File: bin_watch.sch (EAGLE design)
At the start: 90 parts, among them IC1 MEGA48/88/168-AU, J1 USB3100-XX-X_REVB, Q1 32.768kHz, T1 2N7002BKV, T2 2N7002BKV, T3 2N7002BKV, T4 2N7002BKV, T5 PMDT670UPE, T6 PMDT670UPE, T7 PMDT670UPE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

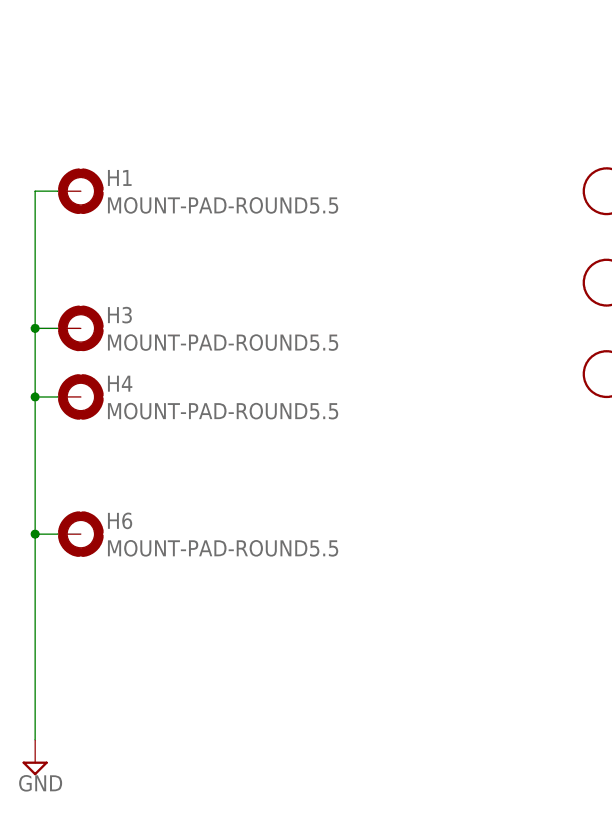
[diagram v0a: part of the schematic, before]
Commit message: Removed mounting holes
Saved a lot more space
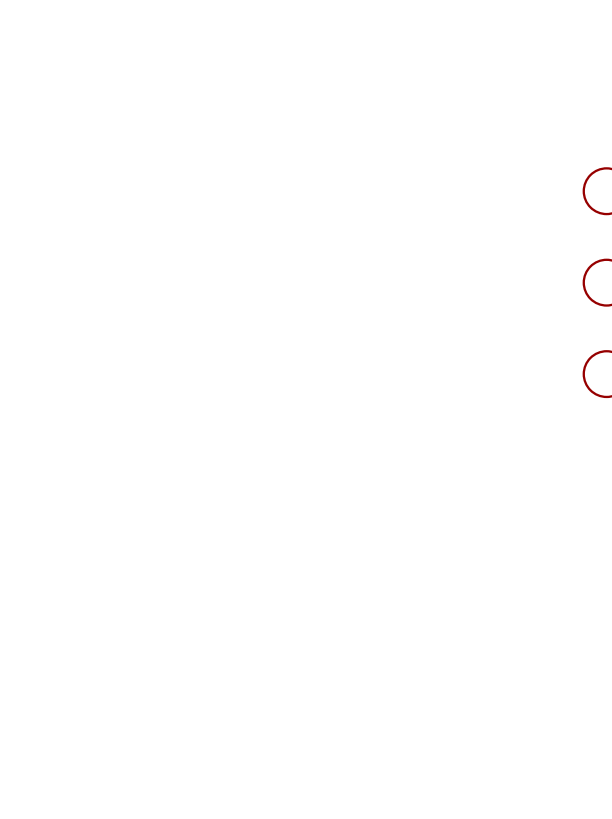
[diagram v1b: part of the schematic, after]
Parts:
- removed H1, H3, H4, H6: MOUNT-PAD-ROUND5.5, holes:MOUNT-PAD-ROUND5.5
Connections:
- net GND: no longer H1.MOUNT, H3.MOUNT, H4.MOUNT, H6.MOUNT
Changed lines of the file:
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@@
 <part name="SUPPLY14" library="supply2" library_urn="urn:adsk.eagle:library:372" deviceset="GND" device=""/>
 <part name="SUPPLY15" library="supply2" library_urn="urn:adsk.eagle:library:372" deviceset="GND" device=""/>
-<part name="H1" library="holes" library_urn="urn:adsk.eagle:library:237" deviceset="MOUNT-PAD-ROUND" device="5.5" value="MOUNT-PAD-ROUND5.5"/>
-<part name="H3" library="holes" library_urn="urn:adsk.eagle:library:237" deviceset="MOUNT-PAD-ROUND" device="5.5" value="MOUNT-PAD-ROUND5.5"/>
-<part name="H4" library="holes" library_urn="urn:adsk.eagle:library:237" deviceset="MOUNT-PAD-ROUND" device="5.5" value="MOUNT-PAD-ROUND5.5"/>
-<part name="H6" library="holes" library_urn="urn:adsk.eagle:library:237" deviceset="MOUNT-PAD-ROUND" device="5.5" value="MOUNT-PAD-ROUND5.5"/>
-<part name="SUPPLY16" library="supply2" library_urn="urn:adsk.eagle:library:372" deviceset="GND" device=""/>
 <part name="T1" library="nxp_60" deviceset="2N7002BK" device="V"/>
 <part name="T2" library="nxp_60" deviceset="2N7002BK" device="V"/>
@@
 <instance part="SUPPLY14" gate="GND" x="254" y="20.32"/>
 <instance part="SUPPLY15" gate="GND" x="299.72" y="223.52"/>
-<instance part="H1" gate="G$1" x="30.48" y="-53.34"/>
-<instance part="H3" gate="G$1" x="30.48" y="-68.58"/>
-<instance part="H4" gate="G$1" x="30.48" y="-76.2"/>
-<instance part="H6" gate="G$1" x="30.48" y="-91.44"/>
-<instance part="SUPPLY16" gate="GND" x="25.4" y="-116.84"/>
 <instance part="T1" gate="-1" x="180.34" y="45.72"/>
 <instance part="T1" gate="-2" x="190.5" y="27.94"/>
@@
 </segment>
 <segment>
-<pinref part="H1" gate="G$1" pin="MOUNT"/>
-<wire x1="27.94" y1="-53.34" x2="25.4" y2="-53.34" width="0.1524" layer="91"/>
-<pinref part="SUPPLY16" gate="GND" pin="GND"/>
-<wire x1="25.4" y1="-53.34" x2="25.4" y2="-68.58" width="0.1524" layer="91"/>
-<wire x1="25.4" y1="-68.58" x2="25.4" y2="-76.2" width="0.1524" layer="91"/>
-<wire x1="25.4" y1="-76.2" x2="25.4" y2="-91.44" width="0.1524" layer="91"/>
-<wire x1="25.4" y1="-91.44" x2="25.4" y2="-114.3" width="0.1524" layer="91"/>
-<pinref part="H3" gate="G$1" pin="MOUNT"/>
-<wire x1="27.94" y1="-68.58" x2="25.4" y2="-68.58" width="0.1524" layer="91"/>
-<junction x="25.4" y="-68.58"/>
-<pinref part="H4" gate="G$1" pin="MOUNT"/>
-<wire x1="27.94" y1="-76.2" x2="25.4" y2="-76.2" width="0.1524" layer="91"/>
-<junction x="25.4" y="-76.2"/>
-<pinref part="H6" gate="G$1" pin="MOUNT"/>
-<wire x1="27.94" y1="-91.44" x2="25.4" y2="-91.44" width="0.1524" layer="91"/>
-<junction x="25.4" y="-91.44"/>
-</segment>
-<segment>

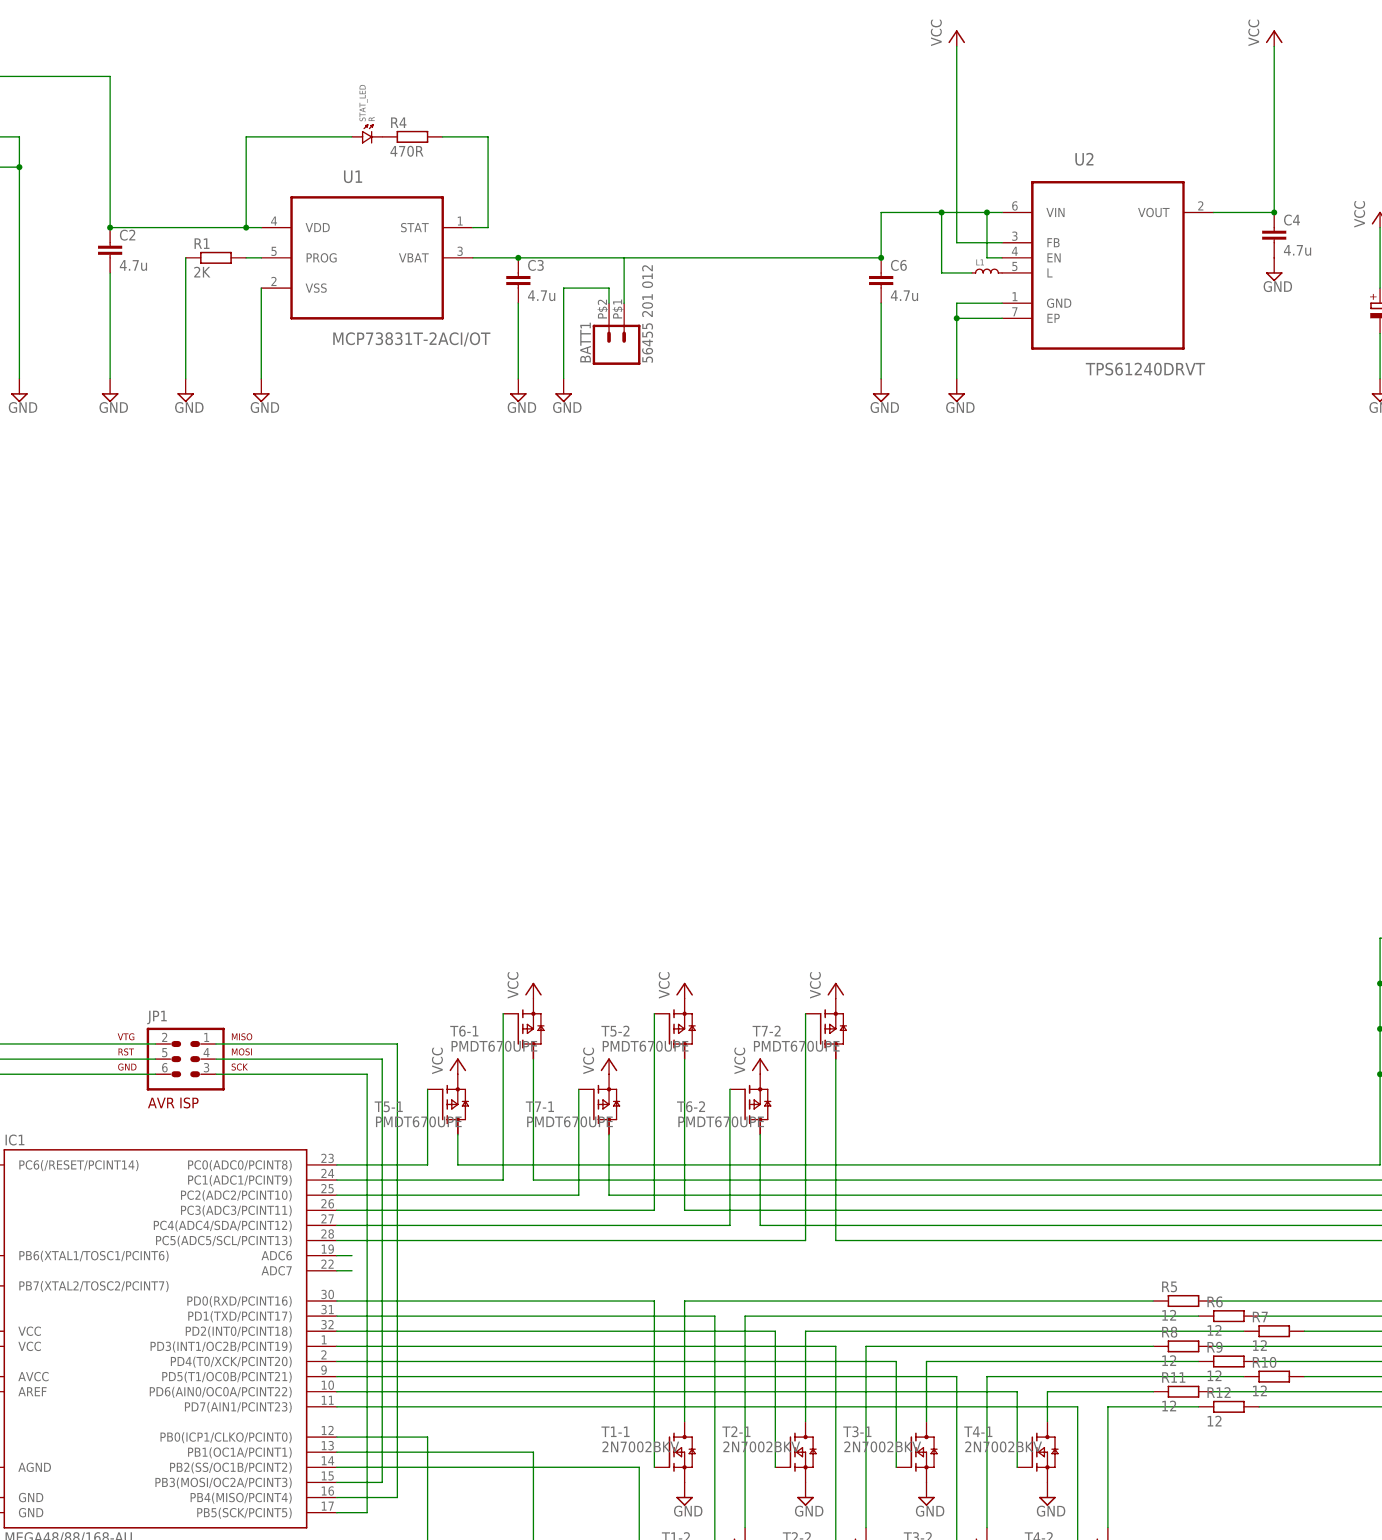
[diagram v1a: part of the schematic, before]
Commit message: Added charger isolation
When the battery is being charged, the Boost converter is powered directly from USB rather than through the charger.
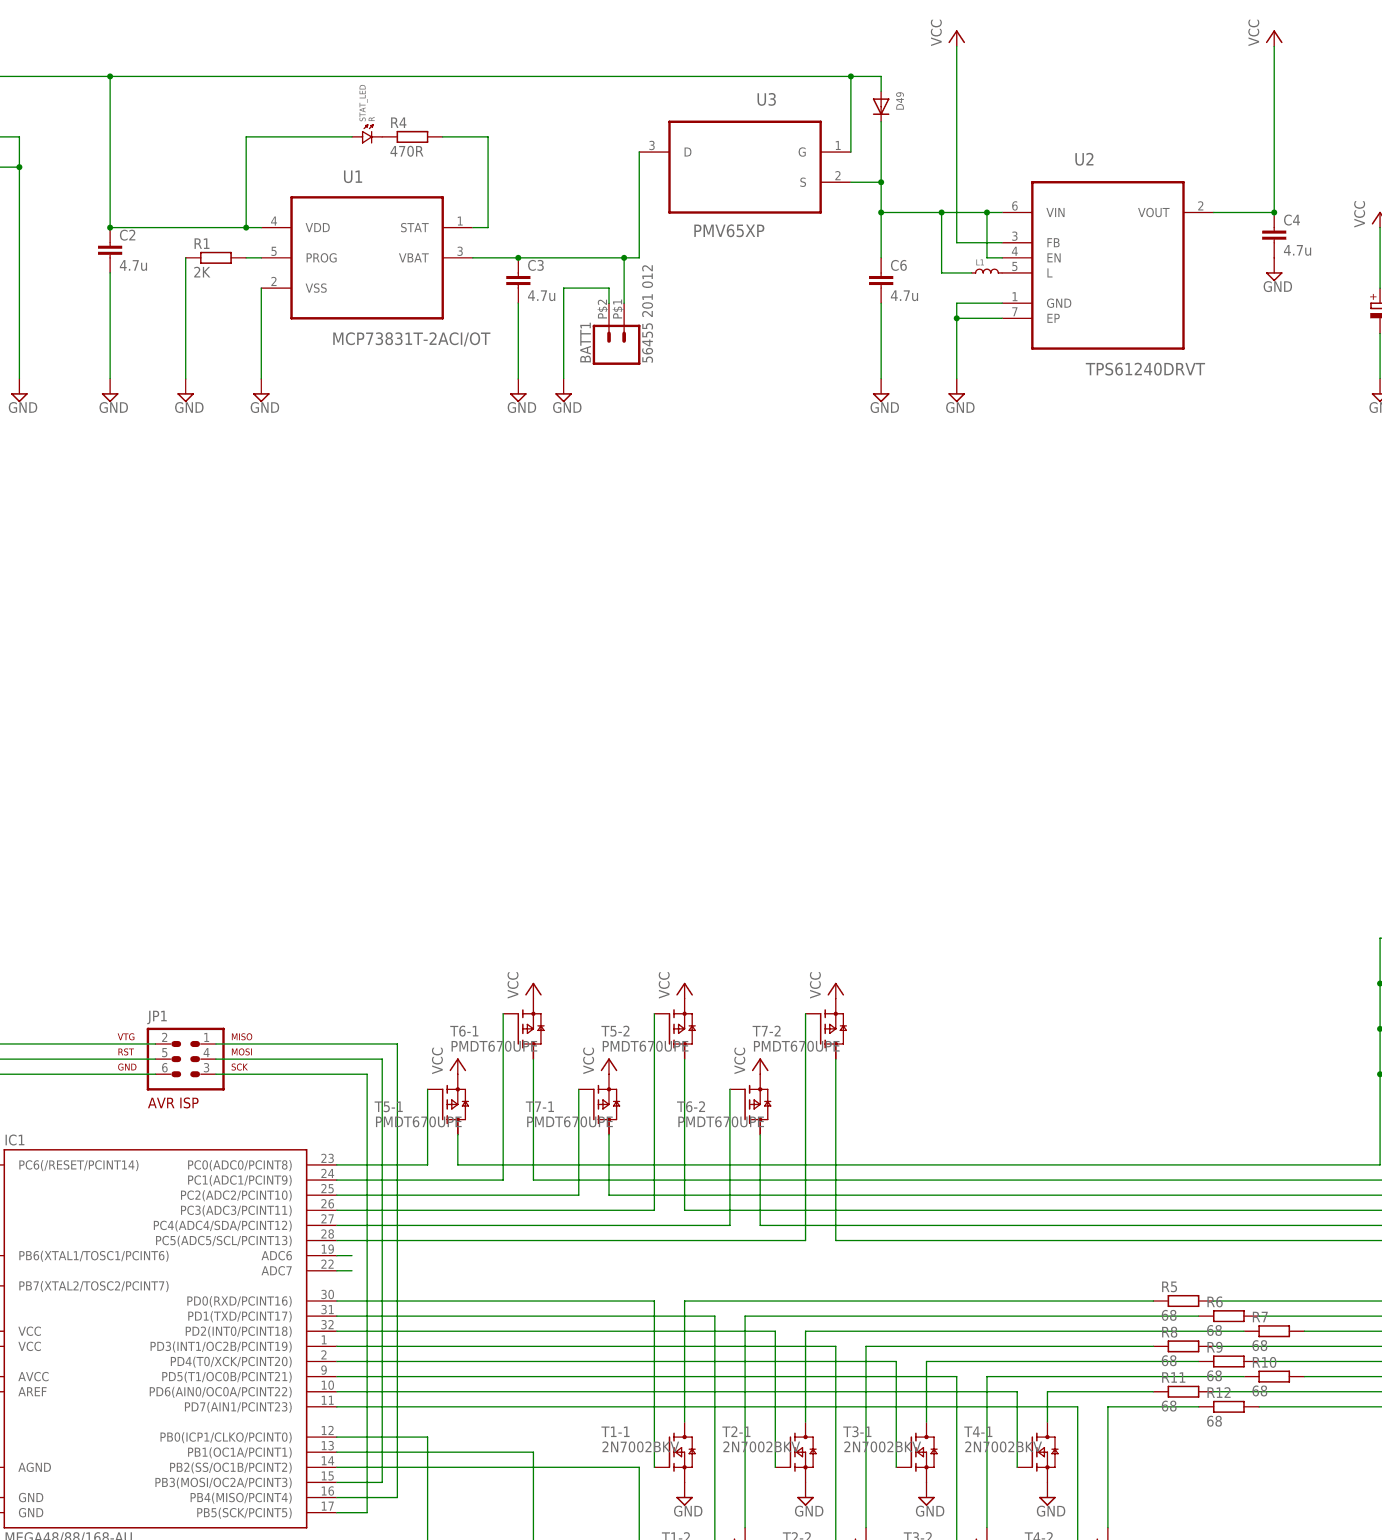
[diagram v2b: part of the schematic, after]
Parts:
- added D49: (no value), adafruit:DIODESOD-523
- added U3: PMV65XP, NXP_By_element14_Batch_1:PMV48XP
- R10, R11, R12, R5, R6, R7, R8, R9: value 12 -> 68
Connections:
- new net VIN: C6.1, D49.C, L1.1, U2.EN, U2.VIN, U3.S
- net VBATT: now also U3.D; no longer C6.1, L1.1, U2.EN, U2.VIN
- net VBUS: now also D49.A, U3.G
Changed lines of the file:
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@@
 <part name="P+9" library="supply1" library_urn="urn:adsk.eagle:library:371" deviceset="VCC" device=""/>
 <part name="C5" library="rcl" library_urn="urn:adsk.eagle:library:334" deviceset="CPOL-EU" device="B/3528-21R" package3d_urn="urn:adsk.eagle:package:23409/1" value="68u"/>
-<part name="R5" library="rcl" library_urn="urn:adsk.eagle:library:334" deviceset="R-EU_" device="R0603" package3d_urn="urn:adsk.eagle:package:23555/1" value="12"/>
-<part name="R6" library="rcl" library_urn="urn:adsk.eagle:library:334" deviceset="R-EU_" device="R0603" package3d_urn="urn:adsk.eagle:package:23555/1" value="12"/>
-<part name="R7" library="rcl" library_urn="urn:adsk.eagle:library:334" deviceset="R-EU_" device="R0603" package3d_urn="urn:adsk.eagle:package:23555/1" value="12"/>
-<part name="R8" library="rcl" library_urn="urn:adsk.eagle:library:334" deviceset="R-EU_" device="R0603" package3d_urn="urn:adsk.eagle:package:23555/1" value="12"/>
-<part name="R9" library="rcl" library_urn="urn:adsk.eagle:library:334" deviceset="R-EU_" device="R0603" package3d_urn="urn:adsk.eagle:package:23555/1" value="12"/>
-<part name="R10" library="rcl" library_urn="urn:adsk.eagle:library:334" deviceset="R-EU_" device="R0603" package3d_urn="urn:adsk.eagle:package:23555/1" value="12"/>
-<part name="R11" library="rcl" library_urn="urn:adsk.eagle:library:334" deviceset="R-EU_" device="R0603" package3d_urn="urn:adsk.eagle:package:23555/1" value="12"/>
-<part name="R12" library="rcl" library_urn="urn:adsk.eagle:library:334" deviceset="R-EU_" device="R0603" package3d_urn="urn:adsk.eagle:package:23555/1" value="12"/>
+<part name="R5" library="rcl" library_urn="urn:adsk.eagle:library:334" deviceset="R-EU_" device="R0603" package3d_urn="urn:adsk.eagle:package:23555/1" value="68"/>
+<part name="R6" library="rcl" library_urn="urn:adsk.eagle:library:334" deviceset="R-EU_" device="R0603" package3d_urn="urn:adsk.eagle:package:23555/1" value="68"/>
+<part name="R7" library="rcl" library_urn="urn:adsk.eagle:library:334" deviceset="R-EU_" device="R0603" package3d_urn="urn:adsk.eagle:package:23555/1" value="68"/>
+<part name="R8" library="rcl" library_urn="urn:adsk.eagle:library:334" deviceset="R-EU_" device="R0603" package3d_urn="urn:adsk.eagle:package:23555/1" value="68"/>
+<part name="R9" library="rcl" library_urn="urn:adsk.eagle:library:334" deviceset="R-EU_" device="R0603" package3d_urn="urn:adsk.eagle:package:23555/1" value="68"/>
+<part name="R10" library="rcl" library_urn="urn:adsk.eagle:library:334" deviceset="R-EU_" device="R0603" package3d_urn="urn:adsk.eagle:package:23555/1" value="68"/>
+<part name="R11" library="rcl" library_urn="urn:adsk.eagle:library:334" deviceset="R-EU_" device="R0603" package3d_urn="urn:adsk.eagle:package:23555/1" value="68"/>
+<part name="R12" library="rcl" library_urn="urn:adsk.eagle:library:334" deviceset="R-EU_" device="R0603" package3d_urn="urn:adsk.eagle:package:23555/1" value="68"/>
 <part name="U$1" library="adafruit" library_urn="urn:adsk.eagle:library:420" deviceset="FIDUCIAL" device=""/>
 <part name="U$2" library="adafruit" library_urn="urn:adsk.eagle:library:420" deviceset="FIDUCIAL" device=""/>
@@
 <part name="L1" library="standardparts" deviceset="RF-INDUCTOR" device=".0805"/>
 <part name="SUPPLY24" library="supply2" library_urn="urn:adsk.eagle:library:372" deviceset="GND" device=""/>
+<part name="U3" library="NXP_By_element14_Batch_1" deviceset="PMV48XP" device="" value="PMV65XP"/>
+<part name="D49" library="adafruit" library_urn="urn:adsk.eagle:library:420" deviceset="DIODE" device="SOD-523"/>
 </parts>
 <sheets>
@@
 <instance part="L1" gate="G$1" x="233.68" y="243.84"/>
 <instance part="SUPPLY24" gate="GND" x="215.9" y="223.52"/>
+<instance part="U3" gate="A" x="193.04" y="264.16" rot="MR0"/>
+<instance part="D49" gate="G$1" x="215.9" y="271.78" rot="R270"/>
 </instances>
 <busses>
@@
 <junction x="86.36" y="251.46"/>
 <pinref part="J1" gate="G$1" pin="VBUS"/>
-</segment>
-</net>
-<net name="VBATT" class="1">
-<segment>
-<pinref part="U1" gate="A" pin="VBAT"/>
-<pinref part="BATT1" gate="G$1" pin="1"/>
-<wire x1="147.32" y1="246.38" x2="154.94" y2="246.38" width="0.1524" layer="91"/>
-<wire x1="154.94" y1="246.38" x2="172.72" y2="246.38" width="0.1524" layer="91"/>
-<wire x1="172.72" y1="246.38" x2="172.72" y2="238.76" width="0.1524" layer="91"/>
-<pinref part="C3" gate="G$1" pin="1"/>
-<junction x="154.94" y="246.38"/>
+<pinref part="U3" gate="A" pin="G"/>
+<wire x1="86.36" y1="276.86" x2="210.82" y2="276.86" width="0.1524" layer="91"/>
+<wire x1="210.82" y1="276.86" x2="210.82" y2="264.16" width="0.1524" layer="91"/>
+<pinref part="D49" gate="G$1" pin="A"/>
+<wire x1="210.82" y1="276.86" x2="215.9" y2="276.86" width="0.1524" layer="91"/>
+<wire x1="215.9" y1="276.86" x2="215.9" y2="274.32" width="0.1524" layer="91"/>
+<junction x="210.82" y="276.86"/>
+<junction x="86.36" y="276.86"/>
+</segment>
+</net>
+<net name="VIN" class="1">
+<segment>
 <pinref part="C6" gate="G$1" pin="1"/>
-<wire x1="172.72" y1="246.38" x2="215.9" y2="246.38" width="0.1524" layer="91"/>
 <wire x1="215.9" y1="246.38" x2="215.9" y2="254" width="0.1524" layer="91"/>
 <pinref part="U2" gate="A" pin="EN"/>
@@
 <wire x1="233.68" y1="246.38" x2="233.68" y2="254" width="0.1524" layer="91"/>
 <wire x1="215.9" y1="254" x2="226.06" y2="254" width="0.1524" layer="91"/>
-<junction x="215.9" y="246.38"/>
 <junction x="233.68" y="254"/>
 <pinref part="L1" gate="G$1" pin="1"/>
@@
 <wire x1="226.06" y1="243.84" x2="226.06" y2="254" width="0.1524" layer="91"/>
 <junction x="226.06" y="254"/>
+<pinref part="U3" gate="A" pin="S"/>
+<wire x1="210.82" y1="259.08" x2="215.9" y2="259.08" width="0.1524" layer="91"/>
+<wire x1="215.9" y1="259.08" x2="215.9" y2="254" width="0.1524" layer="91"/>
+<pinref part="D49" gate="G$1" pin="C"/>
+<wire x1="215.9" y1="269.24" x2="215.9" y2="259.08" width="0.1524" layer="91"/>
+<junction x="215.9" y="254"/>
+<junction x="215.9" y="259.08"/>
 </segment>
 </net>
@@
 </segment>
 </net>
+<net name="VBATT" class="1">
+<segment>
+<pinref part="U3" gate="A" pin="D"/>
+<wire x1="175.26" y1="264.16" x2="175.26" y2="246.38" width="0.1524" layer="91"/>
+<pinref part="BATT1" gate="G$1" pin="1"/>
+<wire x1="172.72" y1="246.38" x2="172.72" y2="238.76" width="0.1524" layer="91"/>
+<wire x1="172.72" y1="246.38" x2="175.26" y2="246.38" width="0.1524" layer="91"/>
+<wire x1="154.94" y1="246.38" x2="172.72" y2="246.38" width="0.1524" layer="91"/>
+<pinref part="C3" gate="G$1" pin="1"/>
+<junction x="154.94" y="246.38"/>
+<pinref part="U1" gate="A" pin="VBAT"/>
+<wire x1="147.32" y1="246.38" x2="154.94" y2="246.38" width="0.1524" layer="91"/>
+<junction x="172.72" y="246.38"/>
+</segment>
+</net>
